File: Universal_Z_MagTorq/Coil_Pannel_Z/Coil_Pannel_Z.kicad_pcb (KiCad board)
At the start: 6 copper layers, 94 x 94 mm, 10 parts, among them J1 2053380002

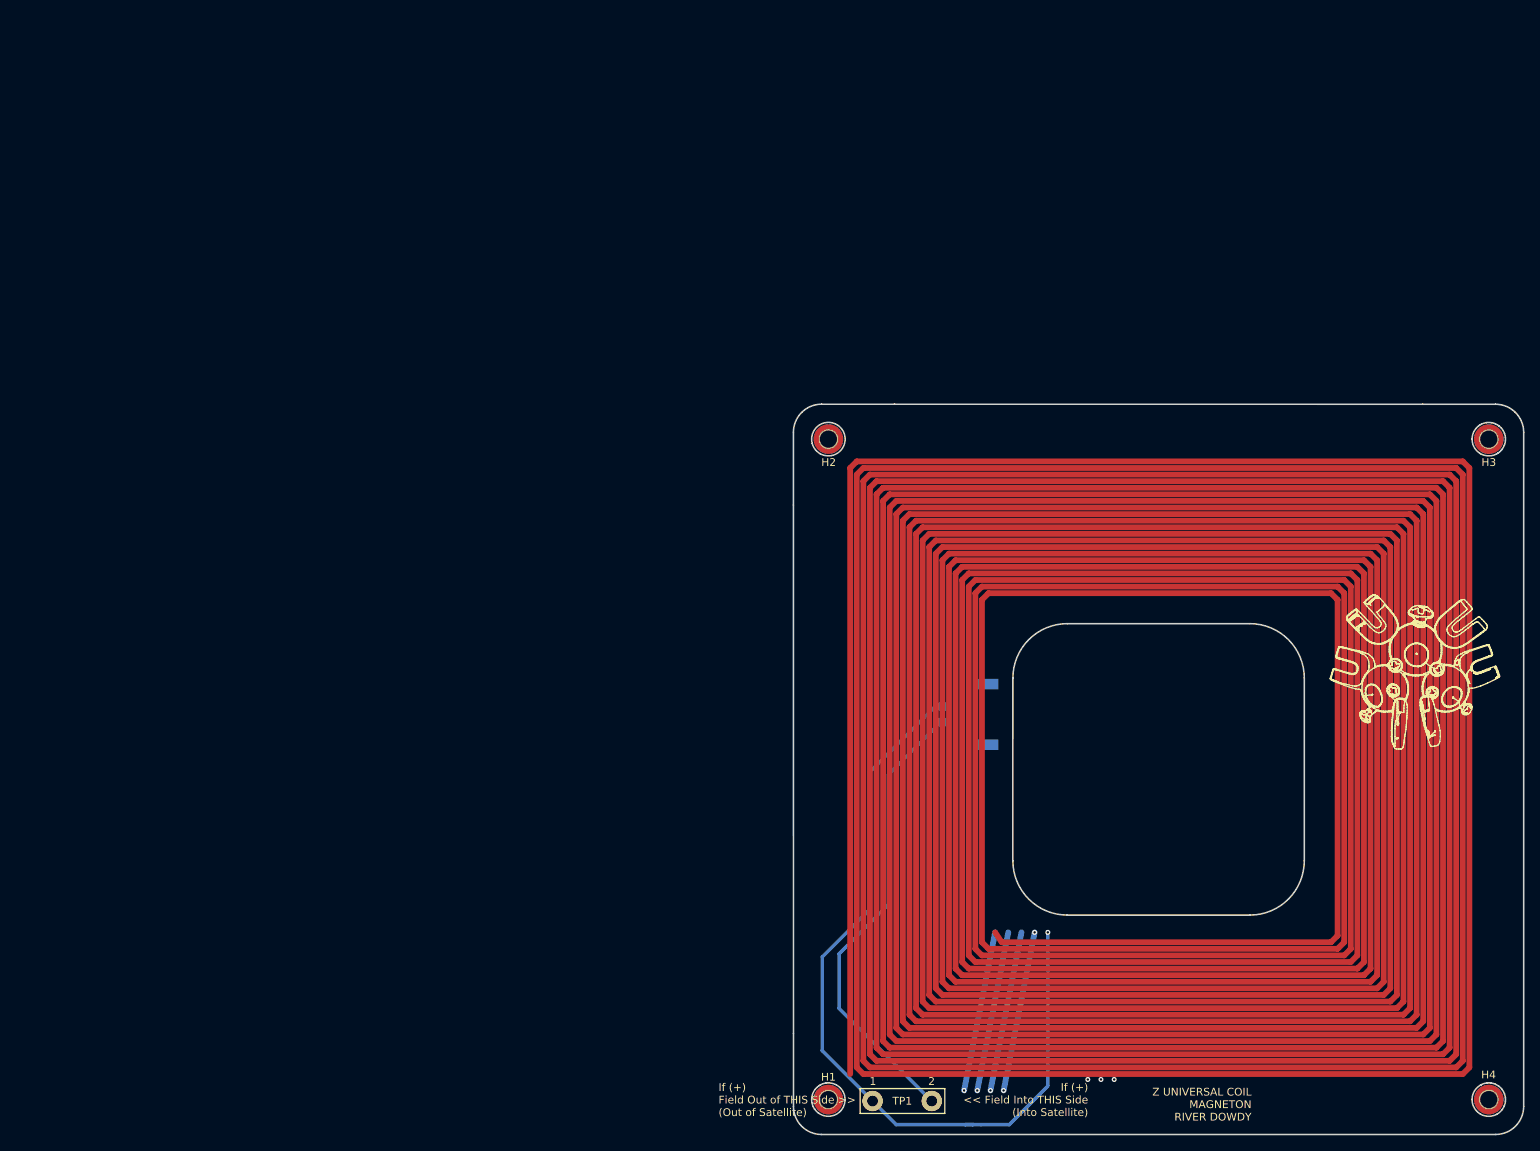
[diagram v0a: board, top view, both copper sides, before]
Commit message: flipped pad for access
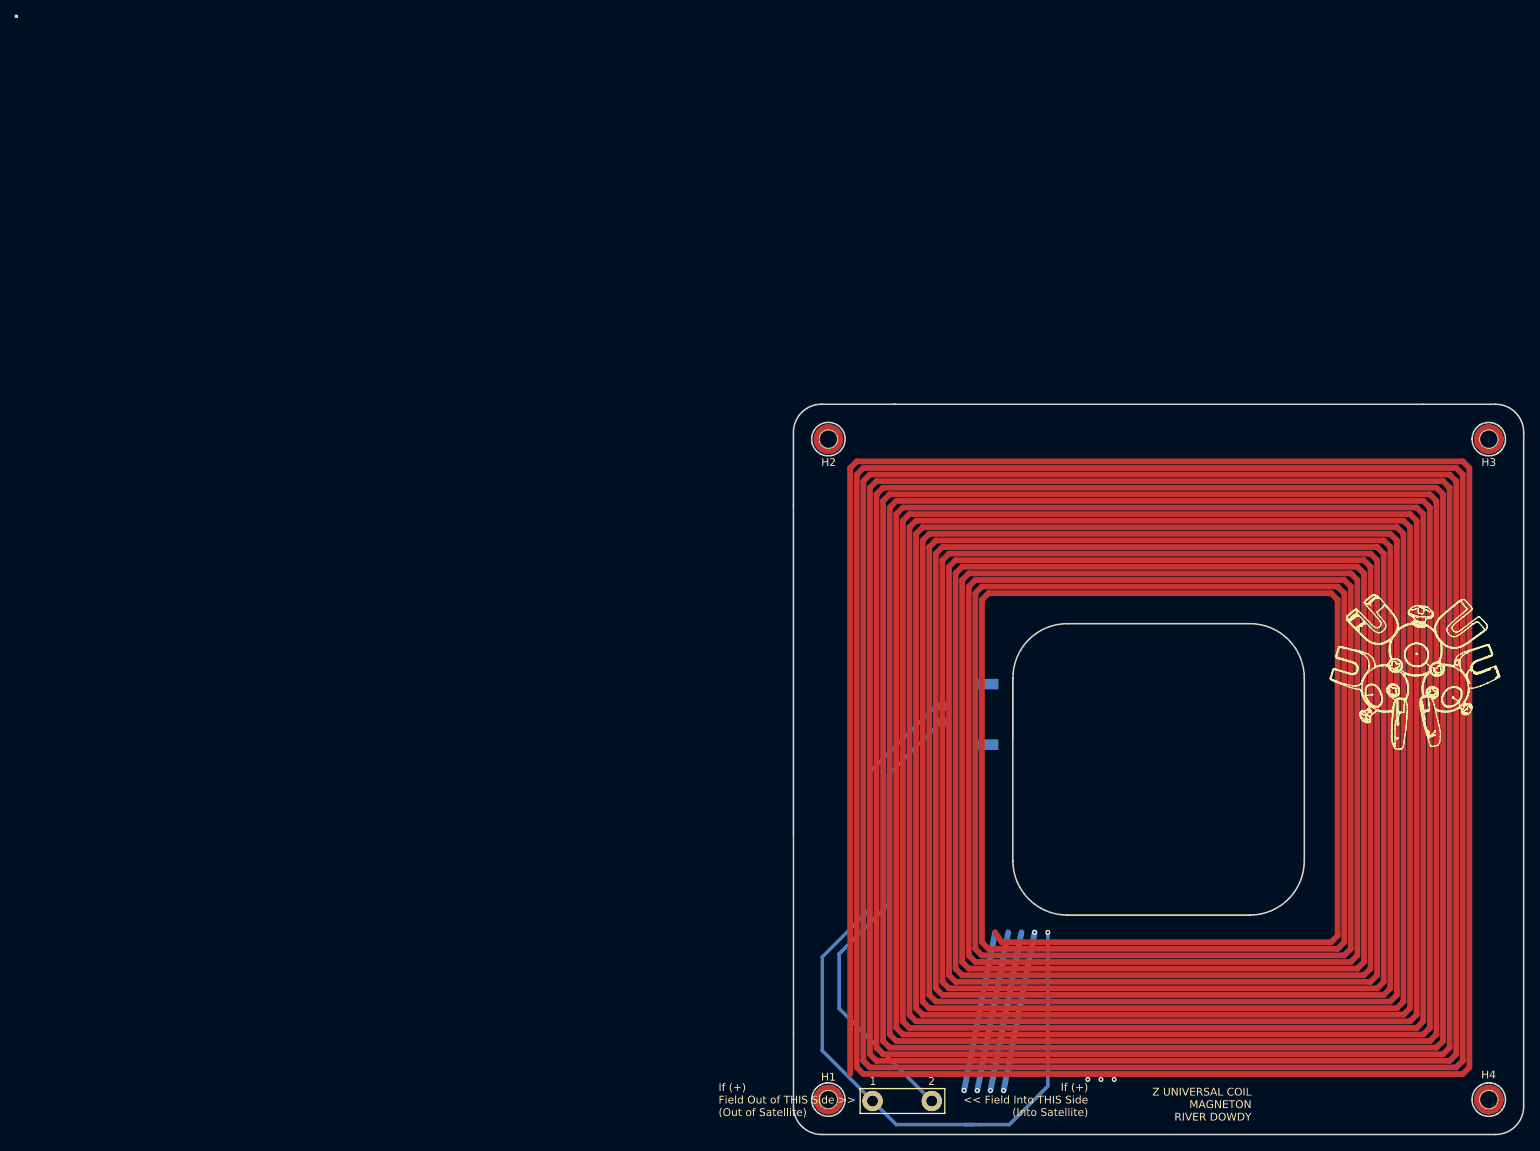
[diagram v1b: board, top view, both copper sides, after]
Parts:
- ? (x2): moved to B.Cu
- moved ? 7.62 mm to (110.3, 139.1), turned to 180 degrees
- moved ? 7.62 mm to (117.9, 139.1), turned to 180 degrees
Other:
- board size 94 x 94 mm -> 194.1 x 144 mm

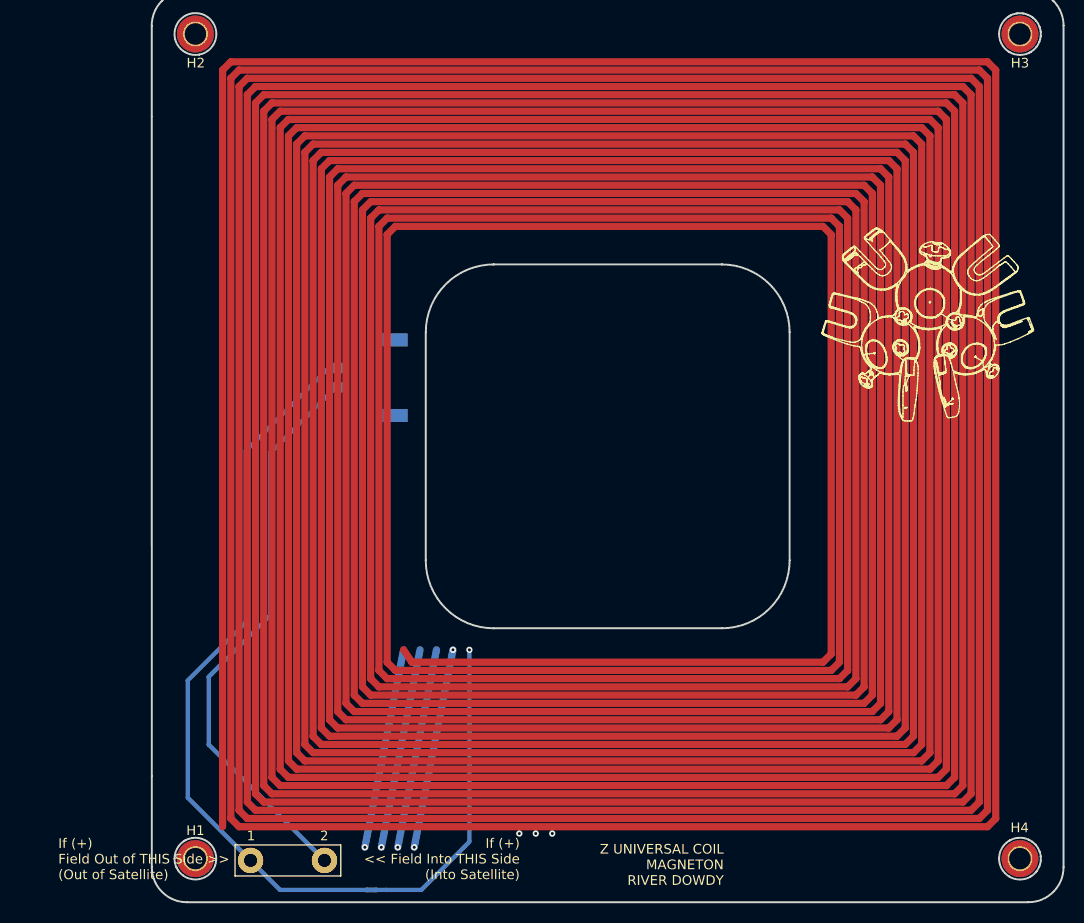
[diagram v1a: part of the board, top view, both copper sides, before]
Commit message: updated t width
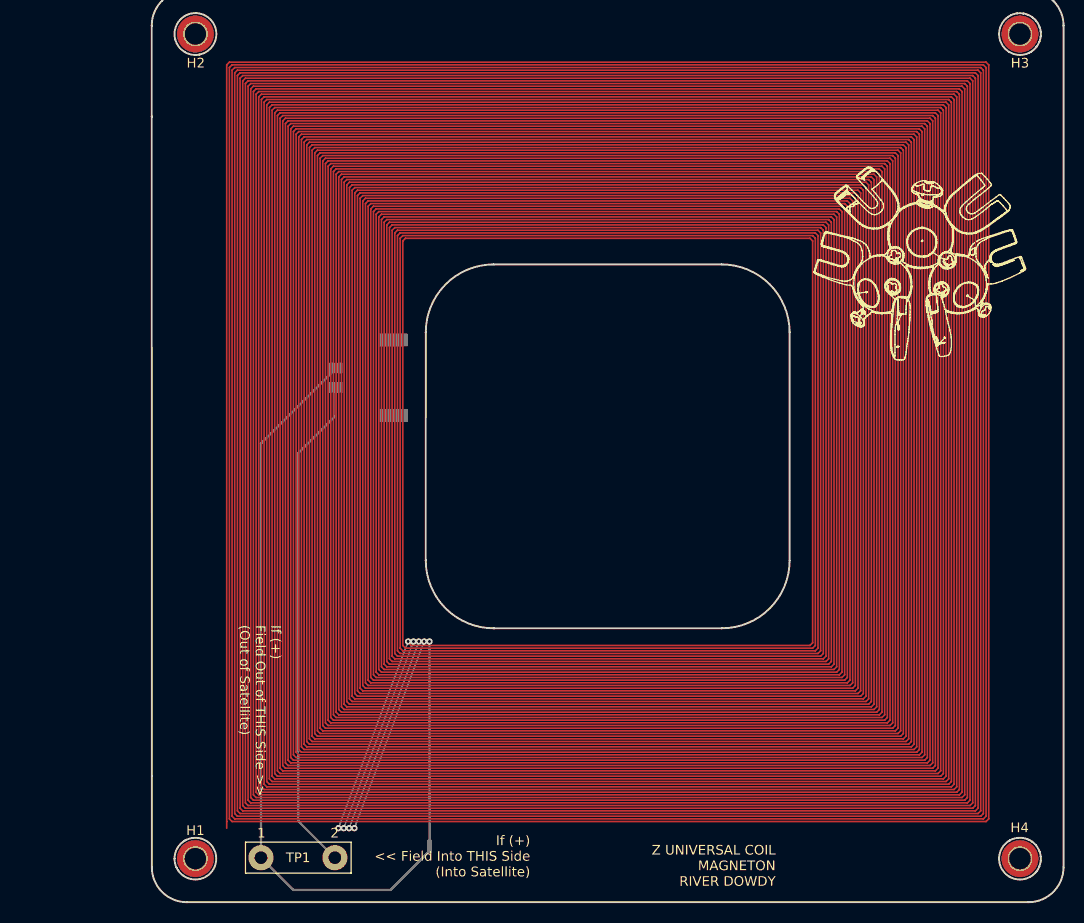
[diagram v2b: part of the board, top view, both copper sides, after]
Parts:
- removed ? (x2): , 
- moved NT1 7.51 mm to (128.8, 137.6), turned to -90 degrees
- moved REF** 6.35 mm to (168.4, 89.6)
- moved TP1 1.11 mm to (115.2, 139.4)
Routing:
- net COIL_2: track 26188.7 -> 80735.4 mm
- net COIL_1: track 72.7 -> 74.1 mm

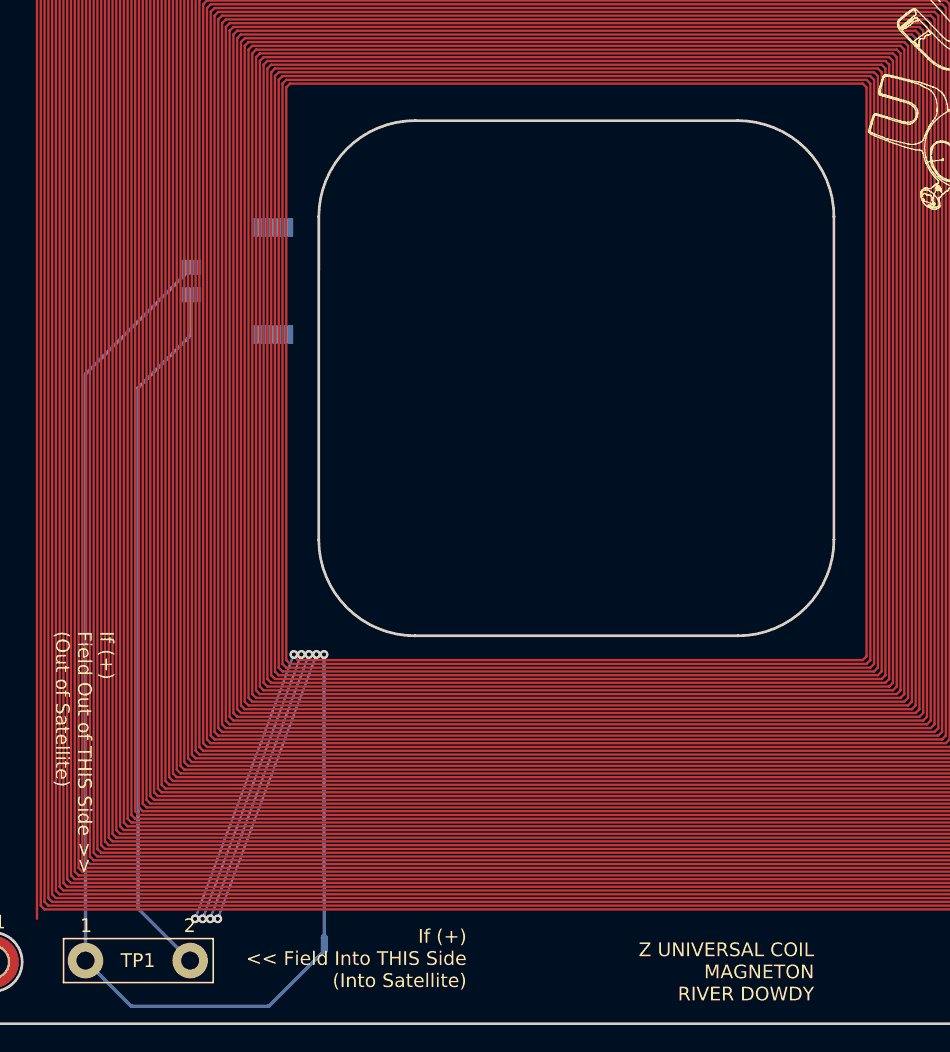
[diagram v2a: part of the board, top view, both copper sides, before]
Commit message: updated spacing to spec
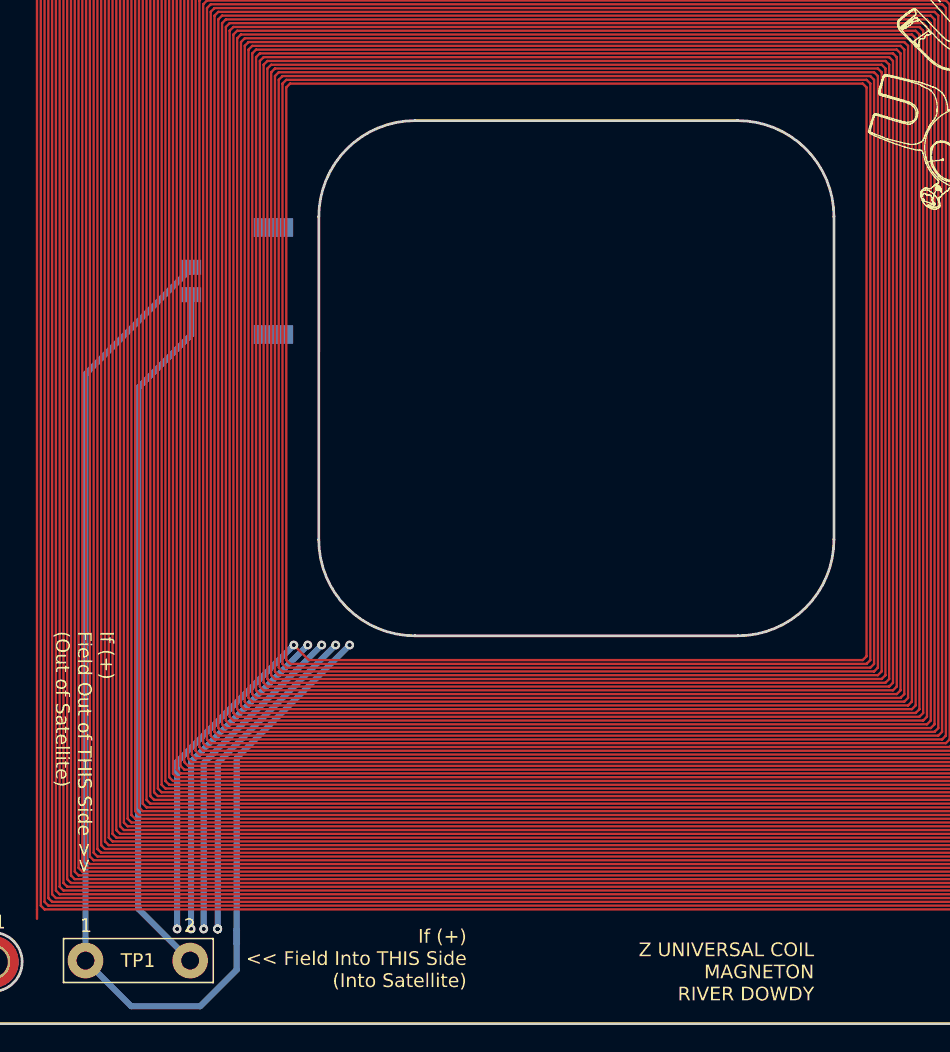
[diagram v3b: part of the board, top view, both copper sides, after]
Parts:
- moved NT1 6.40 mm to (122.4, 137.1)
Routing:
- net COIL_2: track 80735.4 -> 80748.7 mm, vias 9 -> 10
- net COIL_1: track 74.1 -> 69.0 mm
